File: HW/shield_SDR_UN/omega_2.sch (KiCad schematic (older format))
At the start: 17 parts

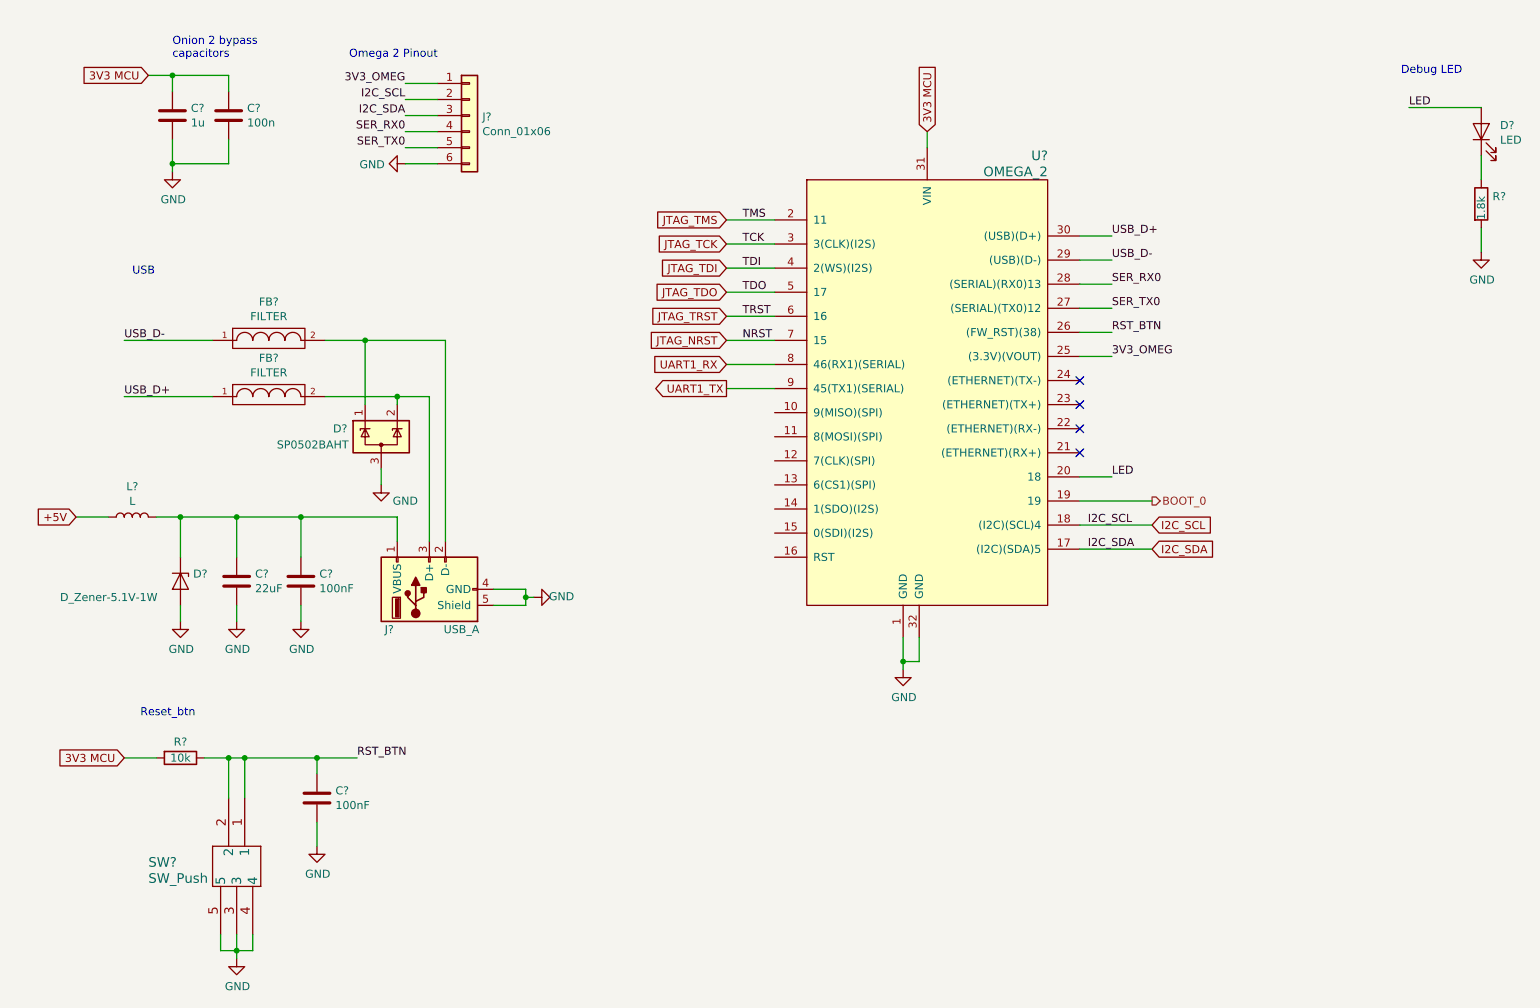
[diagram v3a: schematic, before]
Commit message: se agrego el chip multirelojes
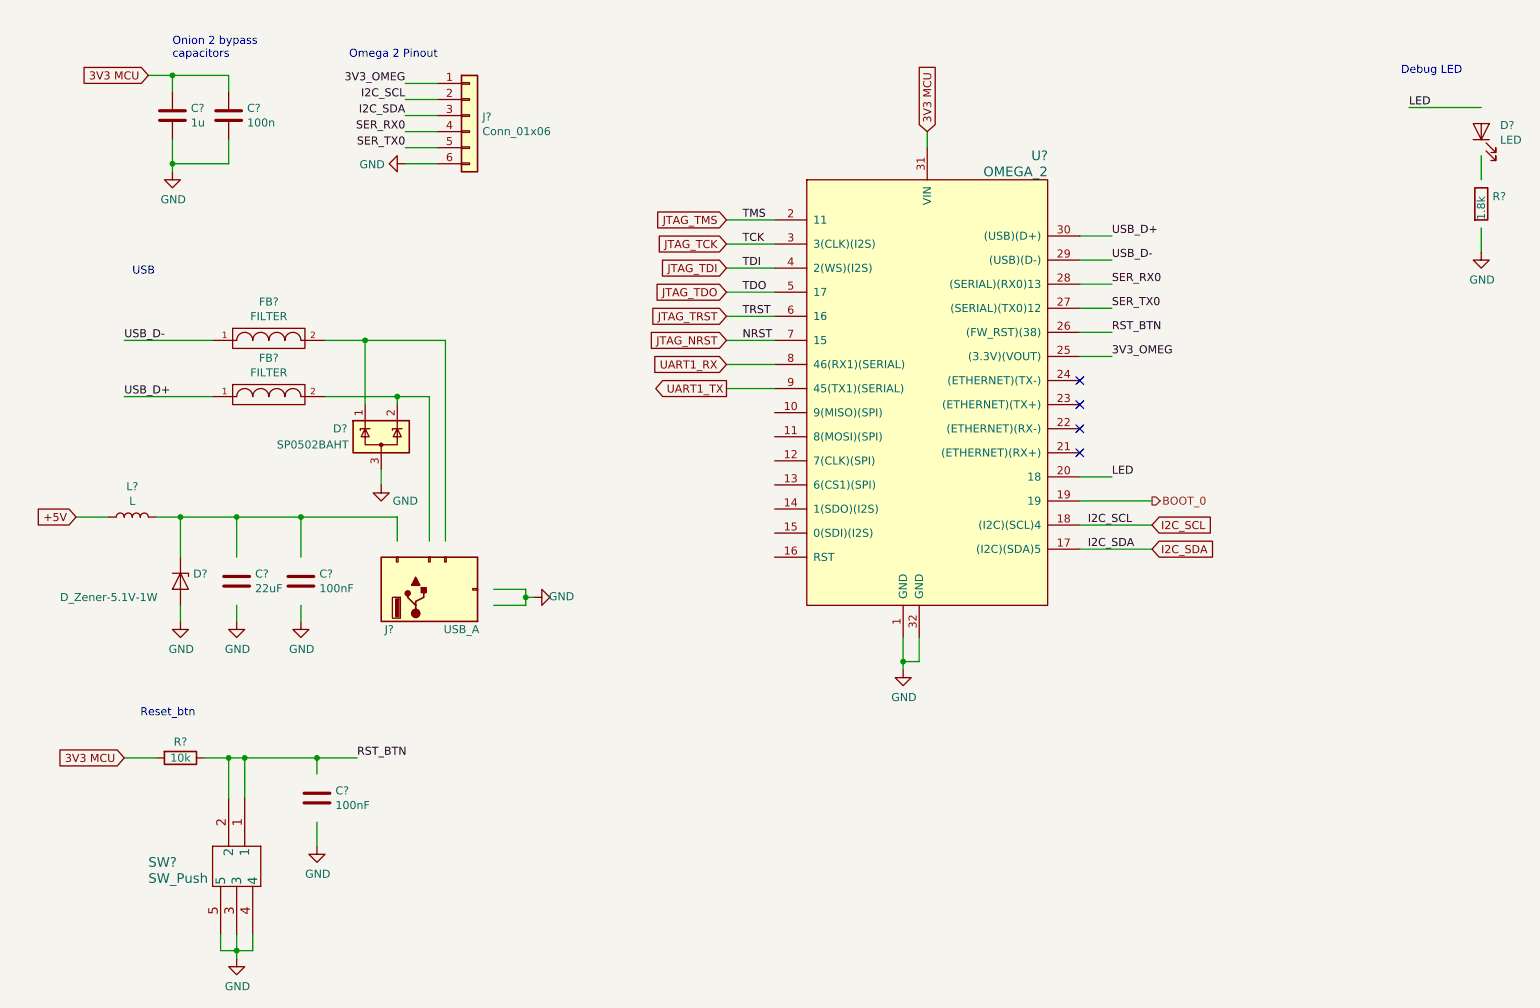
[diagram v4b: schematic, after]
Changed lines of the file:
@@
 $Comp
 L Device:C C?
-U 1 1 5CECC457
+U 0 1 5CECC457
 P 1900 4200
 AR Path="/5CC08321/5CECC457" Ref="C?"  Part="1"
@@
 F 2 "modules:C_0805_HandSoldering" H 1938 4050 50  0001 C CNN
 F 3 "~" H 1900 4200 50  0001 C CNN
-	1    1900 4200
+	0    1900 4200
 	1    0    0    -1
 $EndComp
@@
 $Comp
 L Device:C C?
-U 1 1 5CECC461
+U 0 1 5CECC461
 P 2300 4200
 AR Path="/5CC08321/5CECC461" Ref="C?"  Part="1"
@@
 F 2 "Capacitor_SMD:C_0402_1005Metric" H 2338 4050 50  0001 C CNN
 F 3 "~" H 2300 4200 50  0001 C CNN
-	1    2300 4200
+	0    2300 4200
 	1    0    0    -1
 $EndComp
@@
 $Comp
 L Connector:USB_A J?
-U 1 1 5CECC443
+U 0 1 5CECC443
 P 3100 4250
 AR Path="/5CC08321/5CECC443" Ref="J?"  Part="1"
@@
 F 3 "" H 3250 4200 50  0001 C CNN
 F 4 "https://www.digikey.com/product-detail/en/amphenol-icc-commercial-products/UE27AC54100/UE27AC54100-ND/1972253" H 3100 4250 50  0001 C CNN "digikey"
-	1    3100 4250
+	0    3100 4250
 	0    -1   -1   0
 $EndComp
@@
 $Comp
 L Device:C C?
-U 1 1 5CD83476
+U 0 1 5CD83476
 P 2400 5550
 AR Path="/5CC08321/5CD83476" Ref="C?"  Part="1"
@@
 F 2 "Capacitor_SMD:C_0402_1005Metric" H 2438 5400 50  0001 C CNN
 F 3 "~" H 2400 5550 50  0001 C CNN
-	1    2400 5550
+	0    2400 5550
 	1    0    0    -1
 $EndComp
@@
 $Comp
 L Device:LED D?
-U 1 1 5D35F1A3
+U 0 1 5D35F1A3
 P 9650 1400
 AR Path="/5CC082AD/5D35F1A3" Ref="D?"  Part="1"
@@
 F 2 "LED_SMD:LED_0805_2012Metric_Pad1.15x1.40mm_HandSolder" H 9650 1400 50  0001 C CNN
 F 3 "~" H 9650 1400 50  0001 C CNN
-	1    9650 1400
+	0    9650 1400
 	0    -1   -1   0
 $EndComp
 $Comp
 L Device:R R?
-U 1 1 5D35F1AD
+U 0 1 5D35F1AD
 P 9650 1850
 AR Path="/5CC082AD/5D35F1AD" Ref="R?"  Part="1"
@@
 F 2 "Resistor_SMD:R_0603_1608Metric_Pad1.05x0.95mm_HandSolder" V 9580 1850 50  0001 C CNN
 F 3 "~" H 9650 1850 50  0001 C CNN
-	1    9650 1850
-	1    0    0    -1
-$EndComp
+	0    9650 1850
+	1    0    0    -1
+$EndComp

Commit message: Footprints added for C and R
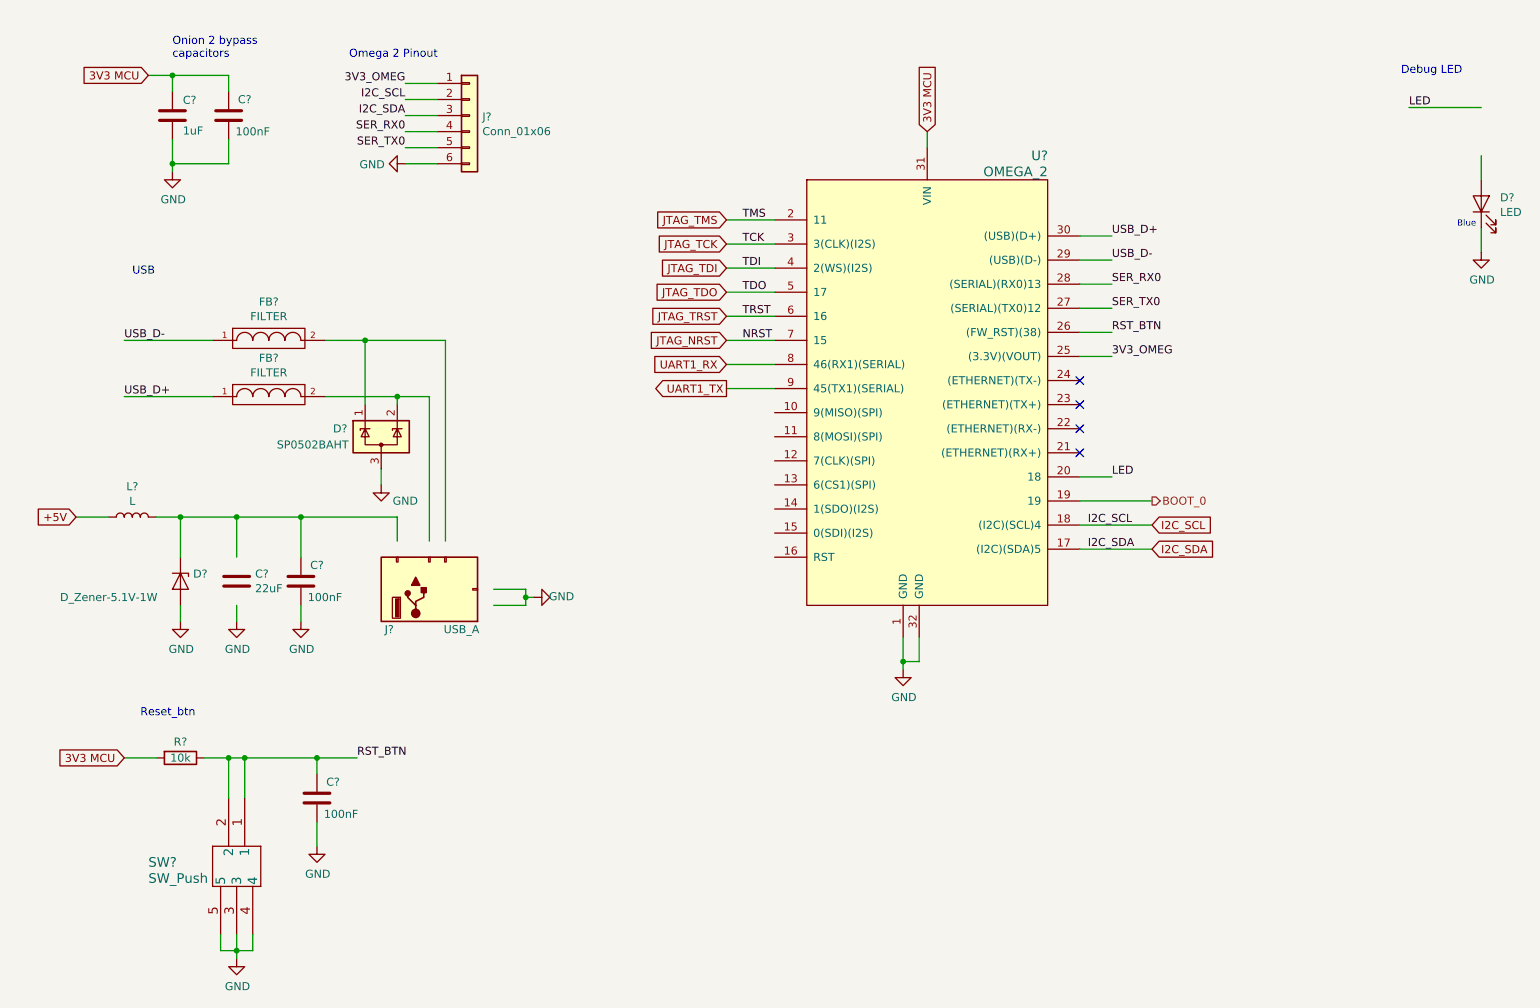
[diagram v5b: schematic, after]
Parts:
- removed C? (x2): 100nF, Capacitor_SMD:C_0402_1005Metric, symbol Device:C
- removed C?: 100n, Capacitor_SMD:C_0402_1005Metric, symbol Device:C
- removed R?: 1.8k, Resistor_SMD:R_0603_1608Metric_Pad1.05x0.95mm_HandSolder, symbol Device:R
- added C? (x3): 100nF, Capacitor_SMD:C_0603_1608Metric_Pad1.05x0.95mm_HandSolder, symbol Device:C
- C?: value 1u -> 1uF; Digikey (none) -> 1276-1182-1-ND
- D?: Digikey (none) -> 160-2032-1-ND
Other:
- note added: "Blue"
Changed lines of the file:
@@
 U 1 1 5CE14EC4
 P 1500 1300
-F 0 "C?" H 1615 1346 50  0000 L CNN
-F 1 "1u" H 1615 1255 50  0000 L CNN
+F 0 "C?" H 1565 1396 50  0000 L CNN
+F 1 "1uF" H 1565 1205 50  0000 L CNN
 F 2 "Capacitor_SMD:C_0402_1005Metric" H 1538 1150 50  0001 C CNN
-F 3 "~" H 1500 1300 50  0001 C CNN
+F 3 "http://www.samsungsem.com/kr/support/product-search/mlcc/__icsFiles/afieldfile/2019/05/10/19-CL10A105KP8NNNC.pdf" H 1500 1300 50  0001 C CNN
+F 4 "1276-1182-1-ND" H 1500 1300 50  0001 C CNN "Digikey"
 	1    1500 1300
-	1    0    0    -1
-$EndComp
-$Comp
-L Device:C C?
-U 1 1 5CE15558
-P 1850 1300
-F 0 "C?" H 1965 1346 50  0000 L CNN
-F 1 "100n" H 1965 1255 50  0000 L CNN
-F 2 "Capacitor_SMD:C_0402_1005Metric" H 1888 1150 50  0001 C CNN
-F 3 "~" H 1850 1300 50  0001 C CNN
-	1    1850 1300
 	1    0    0    -1
 $EndComp
@@
 	1    1550 4200
 	0    1    1    0
-$EndComp
-$Comp
-L Device:C C?
-U 0 1 5CECC461
-P 2300 4200
-AR Path="/5CC08321/5CECC461" Ref="C?"  Part="1"
-AR Path="/5CFB52DC/5CECC461" Ref="C?"  Part="0"
-F 0 "C?" H 2415 4246 50  0000 L CNN
-F 1 "100nF" H 2415 4155 50  0000 L CNN
-F 2 "Capacitor_SMD:C_0402_1005Metric" H 2338 4050 50  0001 C CNN
-F 3 "~" H 2300 4200 50  0001 C CNN
-	0    2300 4200
-	1    0    0    -1
 $EndComp
 $Comp
@@
 Connection ~ 1850 5300
 Connection ~ 1950 5300
-$Comp
-L Device:C C?
-U 0 1 5CD83476
-P 2400 5550
-AR Path="/5CC08321/5CD83476" Ref="C?"  Part="1"
-AR Path="/5CFB52DC/5CD83476" Ref="C?"  Part="0"
-F 0 "C?" H 2515 5596 50  0000 L CNN
-F 1 "100nF" H 2515 5505 50  0000 L CNN
-F 2 "Capacitor_SMD:C_0402_1005Metric" H 2438 5400 50  0001 C CNN
-F 3 "~" H 2400 5550 50  0001 C CNN
-	0    2400 5550
-	1    0    0    -1
-$EndComp
 $Comp
 L power:GND #PWR0202
@@
 $Comp
 L Device:LED D?
-U 0 1 5D35F1A3
-P 9650 1400
+U 1 1 5D35F1A3
+P 9650 1850
 AR Path="/5CC082AD/5D35F1A3" Ref="D?"  Part="1"
-AR Path="/5CFB52DC/5D35F1A3" Ref="D?"  Part="0"
-F 0 "D?" V 9689 1283 50  0000 R CNN
-F 1 "LED" V 9598 1283 50  0000 R CNN
-F 2 "LED_SMD:LED_0805_2012Metric_Pad1.15x1.40mm_HandSolder" H 9650 1400 50  0001 C CNN
-F 3 "~" H 9650 1400 50  0001 C CNN
-	0    9650 1400
+AR Path="/5CFB52DC/5D35F1A3" Ref="D?"  Part="1"
+F 0 "D?" V 9689 1733 50  0000 R CNN
+F 1 "LED" V 9598 1733 50  0000 R CNN
+F 2 "LED_SMD:LED_0805_2012Metric_Pad1.15x1.40mm_HandSolder" H 9650 1850 50  0001 C CNN
+F 3 "http://optoelectronics.liteon.com/upload/download/DS22-2000-239/LTST-S220TBKT.pdf" H 9650 1850 50  0001 C CNN
+F 4 "160-2032-1-ND" V 9650 1850 50  0001 C CNN "Digikey"
+	1    9650 1850
 	0    -1   -1   0
-$EndComp
-$Comp
-L Device:R R?
-U 0 1 5D35F1AD
-P 9650 1850
-AR Path="/5CC082AD/5D35F1AD" Ref="R?"  Part="1"
-AR Path="/5CFB52DC/5D35F1AD" Ref="R?"  Part="0"
-F 0 "R?" H 9720 1896 50  0000 L CNN
-F 1 "1.8k" V 9650 1750 50  0000 L CNN
-F 2 "Resistor_SMD:R_0603_1608Metric_Pad1.05x0.95mm_HandSolder" V 9580 1850 50  0001 C CNN
-F 3 "~" H 9650 1850 50  0001 C CNN
-	0    9650 1850
-	1    0    0    -1
 $EndComp
 $Comp
@@
 Text Label 7350 3550 0    50   ~ 0
 LED
+$Comp
+L Device:C C?
+U 1 1 5D03F2FE
+P 2300 4200
+F 0 "C?" H 2400 4300 50  0000 C CNN
+F 1 "100nF" H 2450 4100 50  0000 C CNN
+F 2 "Capacitor_SMD:C_0603_1608Metric_Pad1.05x0.95mm_HandSolder" H 2338 4050 50  0001 C CNN
+F 3 "http://www.samsungsem.com/kr/support/product-search/mlcc/__icsFiles/afieldfile/2018/07/24/CL10B104KB8NNNC.pdf" H 2300 4200 50  0001 C CNN
+F 4 "1276-1000-1-ND" H 2300 4200 50  0001 C CNN "Digikey"
+	1    2300 4200
+	1    0    0    -1
+$EndComp
+$Comp
+L Device:C C?
+U 1 1 5D040555
+P 2400 5550
+F 0 "C?" H 2500 5650 50  0000 C CNN
+F 1 "100nF" H 2550 5450 50  0000 C CNN
+F 2 "Capacitor_SMD:C_0603_1608Metric_Pad1.05x0.95mm_HandSolder" H 2438 5400 50  0001 C CNN
+F 3 "http://www.samsungsem.com/kr/support/product-search/mlcc/__icsFiles/afieldfile/2018/07/24/CL10B104KB8NNNC.pdf" H 2400 5550 50  0001 C CNN
+F 4 "1276-1000-1-ND" H 2400 5550 50  0001 C CNN "Digikey"
+	1    2400 5550
+	1    0    0    -1
+$EndComp
+$Comp
+L Device:C C?
+U 1 1 5D042D04
+P 1850 1300
+F 0 "C?" H 1950 1400 50  0000 C CNN
+F 1 "100nF" H 2000 1200 50  0000 C CNN
+F 2 "Capacitor_SMD:C_0603_1608Metric_Pad1.05x0.95mm_HandSolder" H 1888 1150 50  0001 C CNN
+F 3 "http://www.samsungsem.com/kr/support/product-search/mlcc/__icsFiles/afieldfile/2018/07/24/CL10B104KB8NNNC.pdf" H 1850 1300 50  0001 C CNN
+F 4 "1276-1000-1-ND" H 1850 1300 50  0001 C CNN "Digikey"
+	1    1850 1300
+	1    0    0    -1
+$EndComp
+Text Notes 9500 2000 0    39   ~ 0
+Blue
 $EndSCHEMATC

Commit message: Footprints updated
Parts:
- added R?: 470, Resistor_SMD:R_0603_1608Metric_Pad1.05x0.95mm_HandSolder, symbol Device:R
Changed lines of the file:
@@
 $EndComp
-Wire Wire Line
-	9650 1250 9200 1250
 Wire Wire Line
 	9650 1550 9650 1700
 Wire Wire Line
 	9650 2000 9650 2150
-Text Label 9200 1250 0    50   ~ 0
+Text Label 9650 1050 0    50   ~ 0
 LED
-Text Notes 9150 1050 0    50   ~ 0
+Text Notes 9350 900  0    50   ~ 0
 Debug LED
 Text Label 7350 3550 0    50   ~ 0
@@
 Text Notes 9500 2000 0    39   ~ 0
 Blue
+Wire Wire Line
+	9650 1050 9650 1250
+$Comp
+L Device:R R?
+U 1 1 5CECF576
+P 9650 1400
+F 0 "R?" H 9700 1450 50  0000 L CNN
+F 1 "470" V 9650 1300 50  0000 L CNN
+F 2 "Resistor_SMD:R_0603_1608Metric_Pad1.05x0.95mm_HandSolder" V 9580 1400 50  0001 C CNN
+F 3 "http://www.yageo.com/documents/recent/PYu-RC_Group_51_RoHS_L_10.pdf" H 9650 1400 50  0001 C CNN
+F 4 "311-470GRCT-ND" V 9650 1400 50  0001 C CNN "Digikey"
+	1    9650 1400
+	1    0    0    -1
+$EndComp
 $EndSCHEMATC

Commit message: Footprints updated
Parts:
- removed C?: 100nF, Capacitor_SMD:C_0603_1608Metric_Pad1.05x0.95mm_HandSolder, symbol Device:C
- removed J?: Conn_01x06, symbol Connector_Generic:Conn_01x06
- removed R?: 10k, Resistor_SMD:R_0603_1608Metric_Pad1.05x0.95mm_HandSolder, symbol Device:R
- removed SW?: SW_Push, SWITCH_FSM1LPA, symbol FSM1LPTR:FSM1LPTR
- added C?: 100nF, Capacitor_SMD:C_0603_1608Metric_Pad1.05x0.95mm_HandSolder, symbol Device:C
- added J?: Conn_02x06_Odd_Even, symbol Connector_Generic:Conn_02x06_Odd_Even
- added R?: 10k, Resistor_SMD:R_0603_1608Metric_Pad1.05x0.95mm_HandSolder, symbol Device:R
- added SW?: SW_Push, SWITCH_FSM1LPA, symbol FSM1LPTR:FSM1LPTR
- C?: footprint modules:C_0805_HandSoldering -> Resistor_SMD:R_0603_1608Metric_Pad1.05x0.95mm_HandSolder; Digikey (none) -> 1276-6504-1-ND
- J?: footprint Connector_USB:USB_Micro-B_GCT_USB3076-30-A -> lib:USB_A_Female_UE27AC54100; Digikey (none) -> UE27AC54100-ND; digikey https://www.digikey.com/product-detail/en/amphenol-icc-comm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 -> (none)
- U?: footprint (none) -> OMEGA2_:OMEGA2_PADS; Digikey (none) -> 2070-OM-O2-ND
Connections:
- net labels added: 3v3 MCU, O_SPI_CLK, O_SPI_CS1, O_SPI_MISO, O_SPI_MOSI
- wire segments 83 -> 93
- no-connect marks 4 -> 7
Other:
- moved on the sheet: U?
